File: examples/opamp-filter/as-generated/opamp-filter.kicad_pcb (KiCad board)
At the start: 2 copper layers, 58 x 42 mm, 22 parts, among them J1 IN, J2 5V, J3 OUT, U1 MCP6001R, U2 MCP6001R

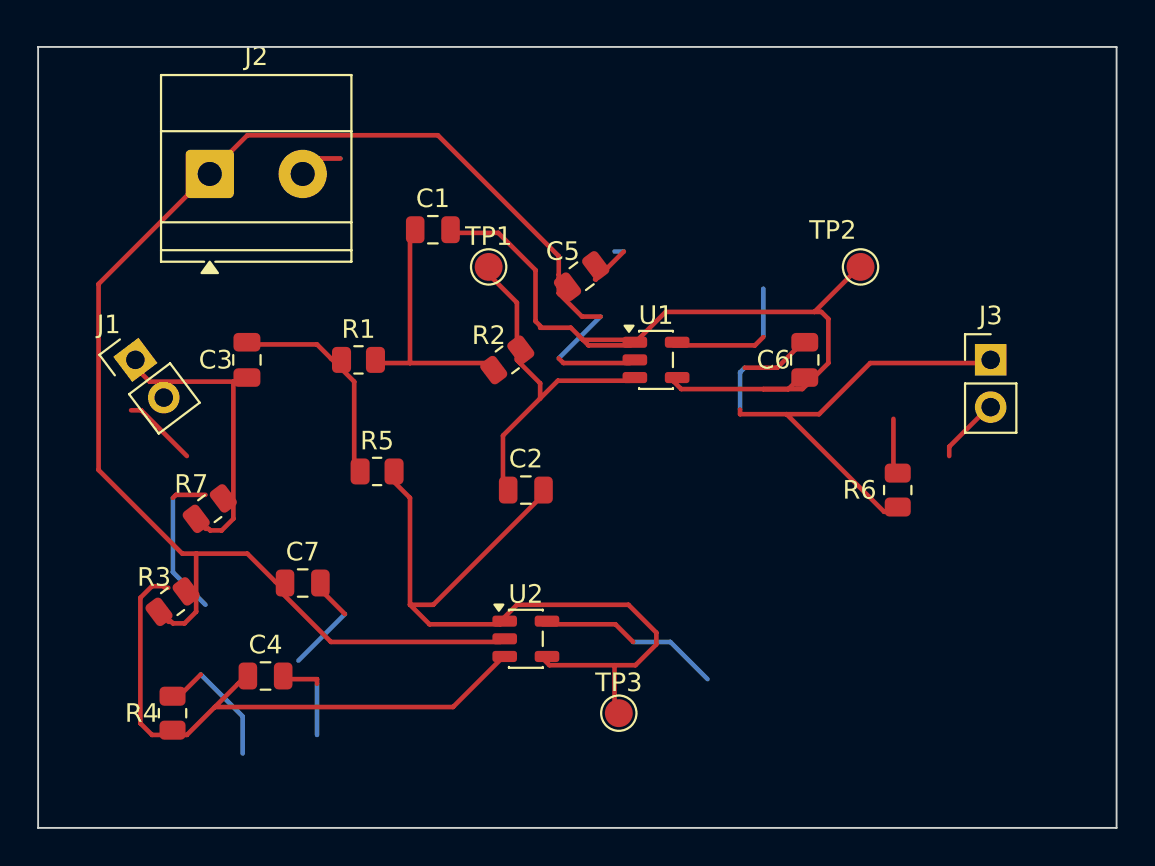
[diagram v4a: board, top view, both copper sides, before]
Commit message: Give the vias room to stand beside the lands
Following the via-in-pad ban, the FPGA board stopped routing: five
attempts, five different nets, each one out of lanes in the corridor
between the FPGA's east escape fan and the codec's west one. Three
changes, in the order a layout would make them.

The via spacing was guesswork and is now the fab's. Hole to hole goes
from 1.2 mm to 0.9, which at the shipped 0.8/0.4 via leaves half a
millimetre of laminate between barrels - the ordinary minimum - and in a
1 mm-pitch escape comb is the difference between a lane and no lane.
What a via keeps off a land it may not sit in is its own radius plus a
solder-mask dam rather than the track clearance: the copper either side
may well be the same net, and what has to be true is that the mask can
part the barrel from the land.

Every decoupling capacitor now has its ground via placed against its own
pad rather than nine of them asking the search for one, and where the
via goes is chosen rather than fixed: `anchor_site` takes the nearest
position that clears everything already placed, fanning either side of
the direction facing off the part. A fixed offset walled off the
corridor its neighbour's supply needed - the via was legal, and it was
in the way.

And the seven parts sitting inside that corridor - four decoupling
capacitors, the two 1.2 V ones and the LED resistor - move four
millimetres south into the empty band below it. Twelve lanes leaving the
FPGA and ten arriving at the codec have eleven millimetres to cross in;
what a hand would do first is stop parking capacitors in the middle of
that, and it is the floorplan half of the debt this board's own README
has been carrying.

Co-Authored-By: Claude Fable 5 <noreply@anthropic.com>
Claude-Session: https://claude.ai/code/session_01DUj7Ltu92tWg159mCSacwY
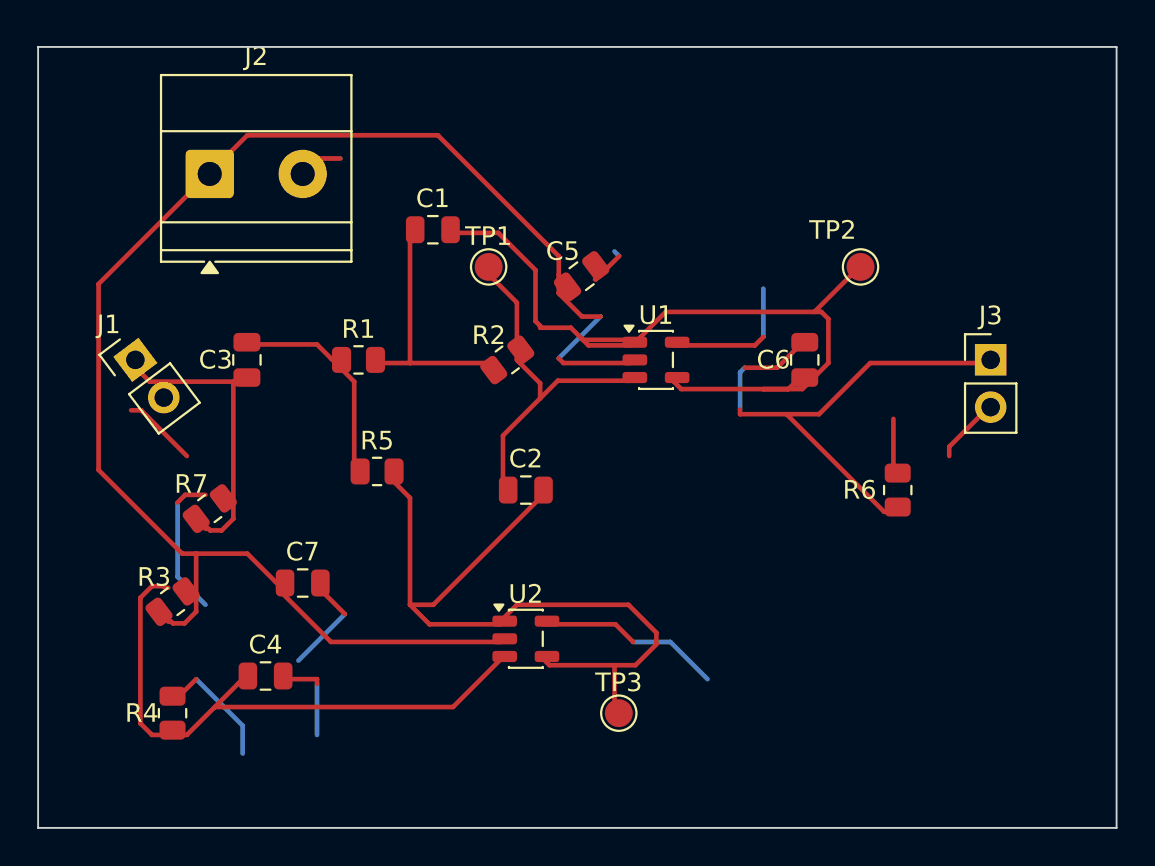
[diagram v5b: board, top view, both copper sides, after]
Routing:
- net GND: track 62.3 -> 60.8 mm
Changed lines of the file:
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@@
 	(segment (start 149.0 81.5) (end 149.0 82.0) (width 0.25) (layer "F.Cu") (net 1))
 	(segment (start 146.0 83.0875) (end 146.0 80.0) (width 0.25) (layer "F.Cu") (net 1))
-	(segment (start 109.0 84.0875) (end 107.4125 84.0875) (width 0.25) (layer "F.Cu") (net 1))
-	(segment (start 107.4125 84.0875) (end 107.25 84.25) (width 0.25) (layer "F.Cu") (net 1))
-	(segment (start 107.25 84.25) (end 107.25 88.25) (width 0.25) (layer "B.Cu") (net 1))
-	(segment (start 107.25 88.25) (end 109.0 90.0) (width 0.25) (layer "B.Cu") (net 1))
+	(segment (start 109.0 84.0875) (end 107.9125 84.0875) (width 0.25) (layer "F.Cu") (net 1))
+	(segment (start 107.9125 84.0875) (end 107.5 84.5) (width 0.25) (layer "F.Cu") (net 1))
+	(segment (start 107.5 84.5) (end 107.5 88.5) (width 0.25) (layer "B.Cu") (net 1))
+	(segment (start 107.5 88.5) (end 109.0 90.0) (width 0.25) (layer "B.Cu") (net 1))
 	(segment (start 114.0 67.0) (end 115.0 66.0) (width 0.25) (layer "F.Cu") (net 1))
 	(segment (start 115.0 66.0) (end 116.25 66.0) (width 0.25) (layer "F.Cu") (net 1))
@@
 	(segment (start 129.95 72.5) (end 130.0 72.5) (width 0.25) (layer "F.Cu") (net 1))
 	(segment (start 130.0 72.5) (end 130.25 72.25) (width 0.25) (layer "F.Cu") (net 1))
-	(segment (start 130.25 72.25) (end 131.5 71.0) (width 0.25) (layer "F.Cu") (net 1))
-	(segment (start 131.5 71.0) (end 131.0 71.0) (width 0.25) (layer "B.Cu") (net 1))
+	(segment (start 130.25 72.25) (end 131.25 71.25) (width 0.25) (layer "F.Cu") (net 1))
+	(segment (start 131.25 71.25) (end 131.0 71.0) (width 0.25) (layer "B.Cu") (net 1))
 	(segment (start 114.95 89.0) (end 115.0 89.0) (width 0.25) (layer "F.Cu") (net 1))
 	(segment (start 115.0 89.0) (end 115.25 89.25) (width 0.25) (layer "F.Cu") (net 1))
@@
 	(segment (start 107.0 95.0) (end 107.25 94.75) (width 0.25) (layer "F.Cu") (net 1))
 	(segment (start 107.25 94.75) (end 107.75 94.75) (width 0.25) (layer "F.Cu") (net 1))
-	(segment (start 107.75 94.75) (end 108.75 93.75) (width 0.25) (layer "F.Cu") (net 1))
-	(segment (start 108.75 93.75) (end 111.0 96.0) (width 0.25) (layer "B.Cu") (net 1))
-	(segment (start 111.0 96.0) (end 111.0 98.0) (width 0.25) (layer "B.Cu") (net 1))
+	(segment (start 107.75 94.75) (end 108.5 94.0) (width 0.25) (layer "F.Cu") (net 1))
+	(segment (start 108.5 94.0) (end 111.0 96.5) (width 0.25) (layer "B.Cu") (net 1))
+	(segment (start 111.0 96.5) (end 111.0 98.0) (width 0.25) (layer "B.Cu") (net 1))
 	(segment (start 139.0 75.6) (end 139.0 73.0) (width 0.25) (layer "B.Cu") (net 1))
 	(segment (start 132.0 92.0) (end 134.0 92.0) (width 0.25) (layer "B.Cu") (net 1))

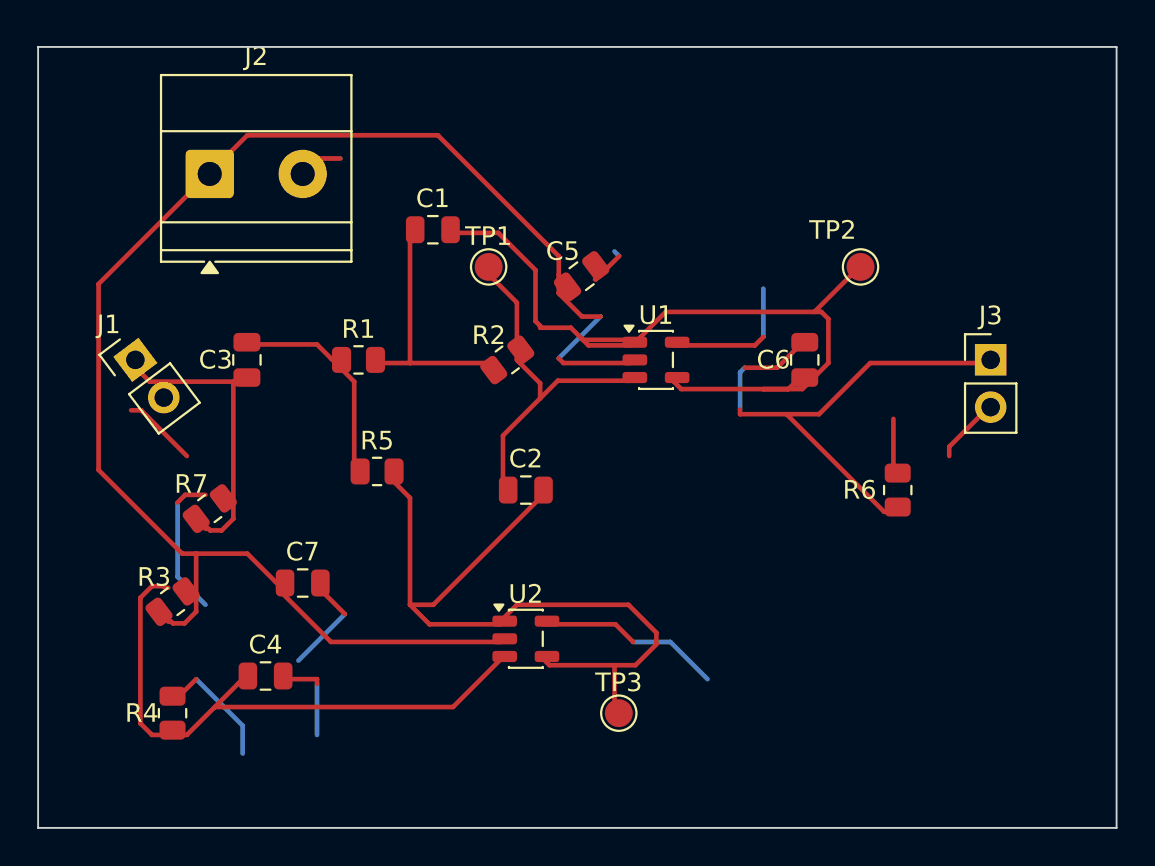
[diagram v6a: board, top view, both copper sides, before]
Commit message: Relieve the pads, fillet the joints, and give the board its screw holes
Three of the reviewer's manufacturing points, and they largely fall out
of the one before it - once KiCad fills the plane, the thermal relief it
was already asked for in the file actually appears.

**Thermal relief.** The zones said thermal all along; our own filler
ignored it and flooded every land solid. KiCad's does not, so every
through-hole ground pad now sits in a gap bridged by four spokes and an
iron can bring the joint up without heating a hundred square millimetres
of copper. `layout.solid_pad_connection` reports the setting when a
board turns it off: drilled pads only, because a surface pad reflows in
an oven that is heating the plane anyway and flooding it is often the
better thermal answer.

**Teardrops.** A track entering a land is a step change in width, and a
step change is where copper tears - the connector gets levered on and
off, the drill wanders, and the crack starts at the corner. `_teardrops`
replaces the first stretch of each run with a three-step taper into the
land, checked against its neighbours before it is kept, so a fillet
never eats the clearance a fine-pitch escape needs. It *replaces* rather
than overlays: laying the taper on top of the run drew the same copper
twice, and `route.acute_angle` reported all thirty of them, correctly.
`route.mixed_track_widths` learns what a fillet looks like so a properly
filleted board does not read as one nobody decided the width of.

**Mounting holes.** Four M3 holes near the corners, placed before the
router runs because they are obstacles, and slid along the edges or a
little inboard where a connector body has the corner - the motor board
and the op-amp take three, which is what those floorplans have room for.
Grounded on the motor driver, whose chassis is metal and part of the
shield, plain on the rest: bonding the enclosure to the reference is the
enclosure's decision, not the board's.

Two things that fell out of placing par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
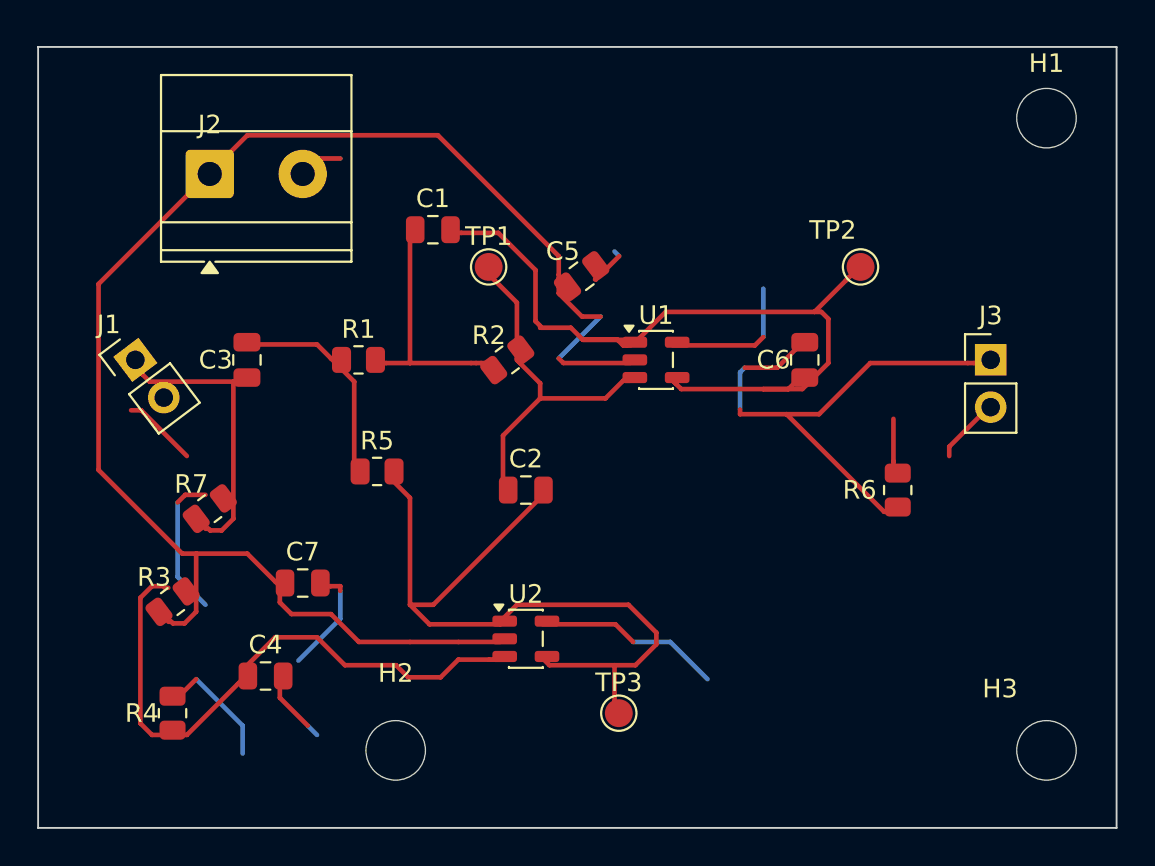
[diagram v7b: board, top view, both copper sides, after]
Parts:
- added H1: M33, MountingHole:MountingHole_3.2mm_M3, F.Cu at (154.2, 63.8)
- added H2: M33, MountingHole:MountingHole_3.2mm_M3, F.Cu at (119.2, 97.8)
- added H3: M33, MountingHole:MountingHole_3.2mm_M3, F.Cu at (154.2, 97.8)
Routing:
- net GND: track 60.8 -> 60.1 mm

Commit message: Give the assembly machine something to aim at
Fiducials: three copper dots in bare mask windows, near three different
corners so a pick-and-place gets rotation as well as offset. It aligns
to the board, not to the drawing - without them it has only the routed
outline, cut to a tolerance ten times looser than the placement a 0.5 mm
pitch part is asking for. `fab.no_fiducials` reports a fine-pitch board
that has none, as context rather than as a fault: plenty of boards are
built one at a time with tweezers.

They share the corner search with the mounting holes, which is where
this found a real bug: `_courtyard_box` read lines and rectangles only,
and a mounting hole draws its courtyard as one circle - so every hole
measured as taking up no room at all, and the first three fiducials
landed on top of three screw holes. Circles and arcs count now.

Co-Authored-By: Claude Fable 5 <noreply@anthropic.com>
Claude-Session: https://claude.ai/code/session_01DUj7Ltu92tWg159mCSacwY
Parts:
- added FID1: Fiducial, Fiducial:Fiducial_1mm_Mask2mm, F.Cu at (102.7, 62.3)
- added FID2: Fiducial, Fiducial:Fiducial_1mm_Mask2mm, F.Cu at (148.7, 62.3)
- added FID3: Fiducial, Fiducial:Fiducial_1mm_Mask2mm, F.Cu at (102.7, 99.3)
- H1, H2, H3: value M33 -> M3
